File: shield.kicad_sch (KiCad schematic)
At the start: 0 parts

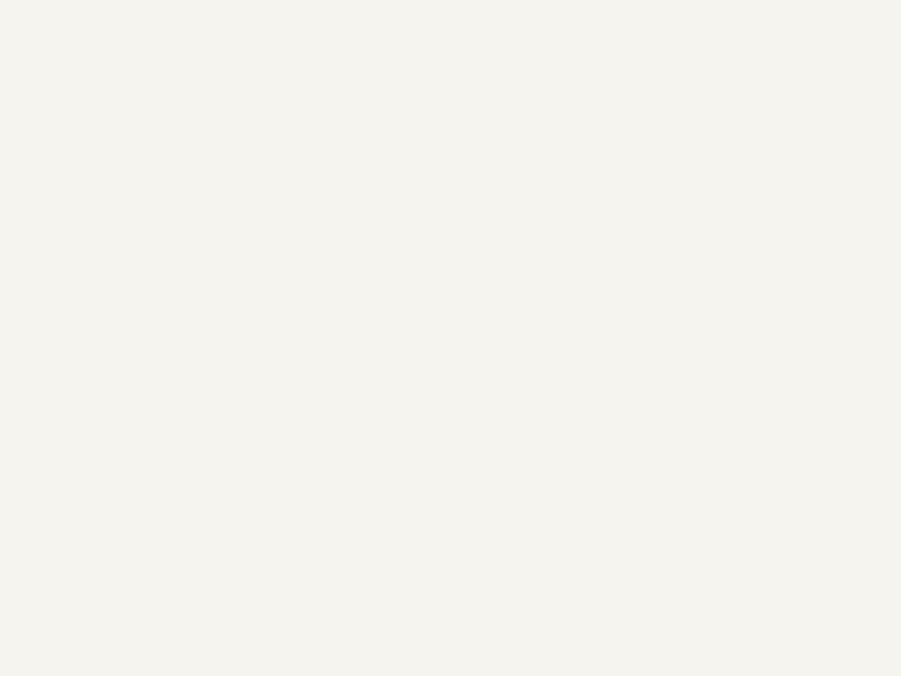
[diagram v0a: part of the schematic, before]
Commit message: Corrige ADC-2 (I_SHUNT1_CMP/I_SHUNT2_CMP) et protege 11 signaux nappe (decisions #18-19)
ADC-2 ne cablait que la voie filtree (I_shunt1/I_shunt2) et oubliait le
chemin direct comparateur que la decision #4 impose. Ajoute en
consommant 2 des 6 reserves, sans adjacence avec la voie filtree (les
deux chemins doivent rester independants).

11 signaux cables en decision #17 n'avaient aucune protection
(CLB_OUT, UART_TX/RX, SPI_CLK/SIMO/SOMI/STE, CAN_TX/RX, et les deux
I_SHUNT*_CMP une fois ajoutes) alors que les 23 autres signaux du
connecteur devkit en ont une. Nouvelle feuille protection_nappe.kicad_sch,
11 trios copies depuis un trio reel (protection_devkit3.kicad_sch) plutot
que redessines - BAT54S + R + 100pF, R=100R standard sauf les deux
I_SHUNT*_CMP a 22R (decision #4 : Rs<=50 Ohm sur ce chemin, 100R le
depasserait).

9 labels renommes en _MCU cote connecteur_devkit.kicad_sch (meme
convention que les 23 trios existants : le nom brut cote nappe, le nom
_MCU cote connecteur devkit, jamais l'inverse).

Egalement loggee : decision #18, le decoupage 100nF des 6 nappes pose
manuellement par l'utilisateur dans une session precedente.

Verifie par kicad-cli sch erc, compare par type de violation : les 11
isolated_pin_label vises ont disparu, aucune autre categorie n'augmente
sauf endpoint_off_grid (+33, un par composant neuf, meme defaut
pre-existant que les 23 trios deja en place).
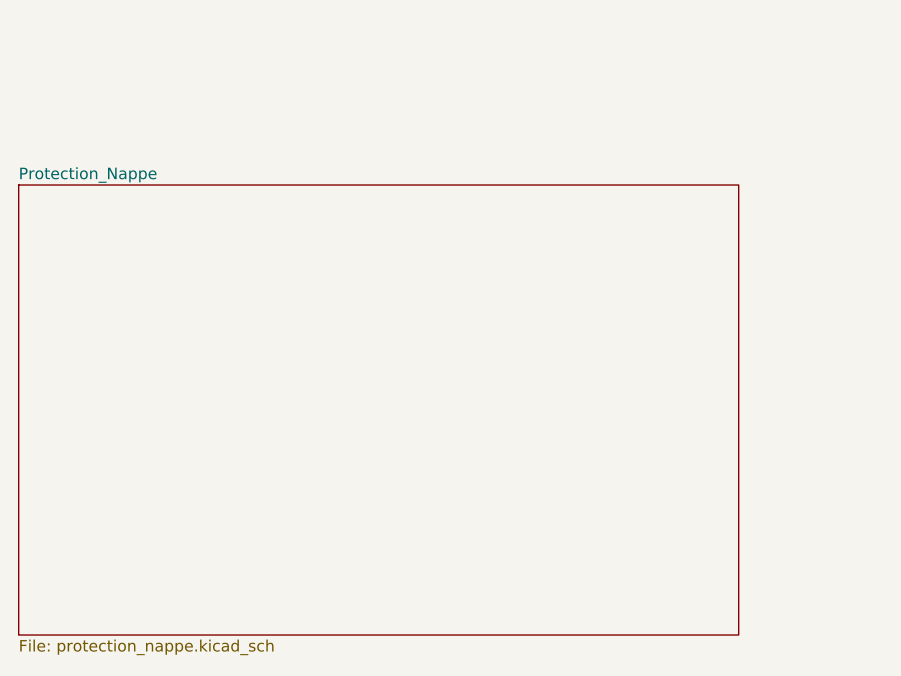
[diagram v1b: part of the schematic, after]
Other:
- added sheet Protection_Nappe (protection_nappe.kicad_sch)
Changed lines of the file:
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@@
+		)
+	)
+	(sheet
+		(at 20 160)
+		(size 80 50)
+		(exclude_from_sim no)
+		(in_bom yes)
+		(on_board yes)
+		(dnp no)
+		(fields_autoplaced yes)
+		(stroke
+			(width 0.1524)
+			(type solid)
+		)
+		(fill
+			(color 0 0 0 0)
+		)
+		(property "Sheetname" "Protection_Nappe"
+			(at 20 159.5 0)
+			(show_name no)
+			(do_not_autoplace no)
+			(effects
+				(font
+					(size 1.27 1.27)
+				)
+				(justify left bottom)
+			)
+		)
+		(property "Sheetfile" "protection_nappe.kicad_sch"
+			(at 20 210.5 0)
+			(show_name no)
+			(do_not_autoplace no)
+			(effects
+				(font
+					(size 1.27 1.27)
+				)
+				(justify left top)
+			)
+		)
+		(instances
+			(project "shield"
+				(path "/3e79b37e-13ed-4a43-b954-3b2f3b716c2c"
+					(page "8")
+				)
+			)
 		)
 	)
